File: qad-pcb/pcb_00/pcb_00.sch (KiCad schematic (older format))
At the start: 19 parts

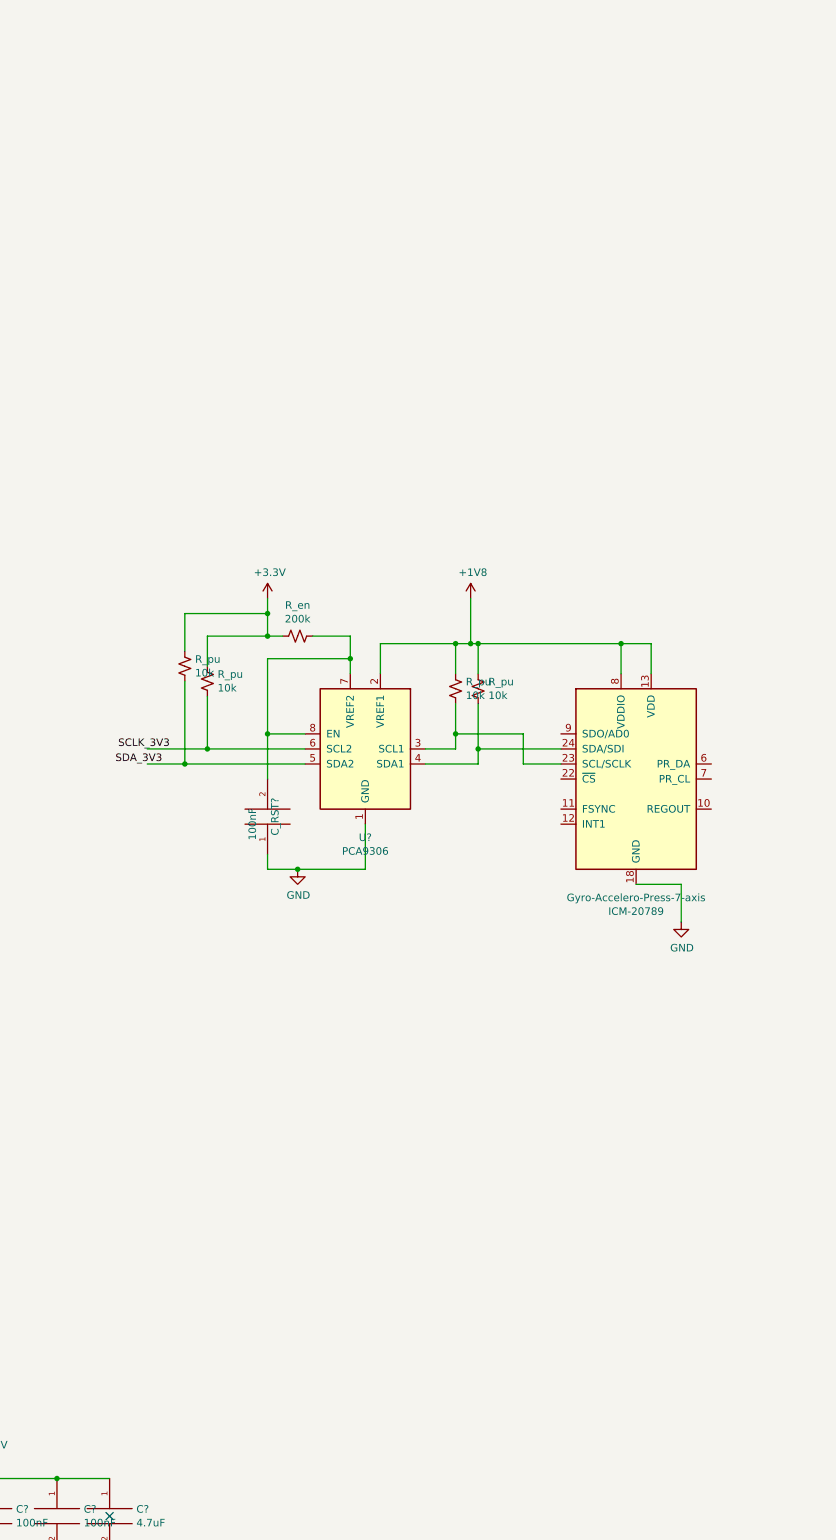
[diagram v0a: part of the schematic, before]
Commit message: Changed IMU :ICM-20789 -> BNO055
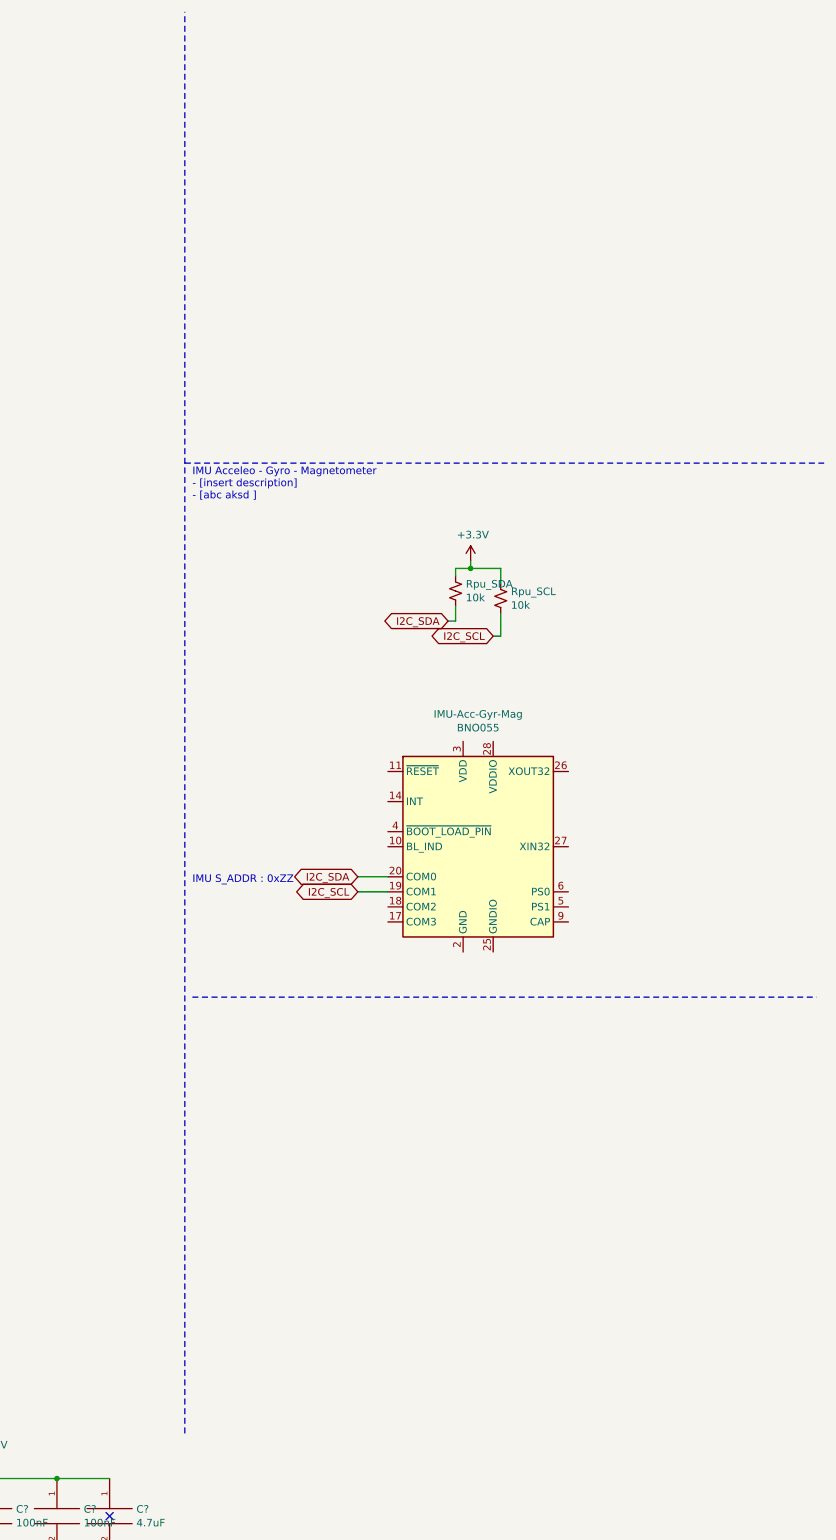
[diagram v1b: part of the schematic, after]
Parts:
- removed C_RST?: 100nF, symbol pspice:CAP
- removed Gyro-Accelero-Press-7-axis: ICM-20789, symbol my-qad-lib:ICM-20789
- removed R_en: 200k, symbol Device:R_Small_US
- removed R_pu (x4): 10k, symbol Device:R_Small_US
- removed U?: PCA9306, symbol Interface:PCA9306
- added IMU-Acc-Gyr-Mag: BNO055, Package_LGA:LGA-28_5.2x3.8mm_P0.5mm, symbol Sensor_Motion:BNO055
- added Rpu_SCL, Rpu_SDA: 10k, symbol Device:R_Small_US
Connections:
- net labels added: I2C_SCL, I2C_SDA
- net labels removed: +1V8, SCLK_3V3, SDA_3V3
- wire segments 82 -> 46
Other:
- note added: "IMU Acceleo - Gyro - Magnetometer\n- [insert description]\n- [abc aksd ]"
- note added: "IMU S_ADDR : 0xZZ"

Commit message: sch updated
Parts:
- gave numbers to parts that had none: 7
- renumbered C_RST to C_RST1, IMU-Acc-Gyr-Mag to IMU-Acc-Gyr-Mag1, R_RST to R_RST2, Rpu_SCL to Rpu_SCL1, Rpu_SDA to Rpu_SDA1, SW_RST to SW_RST1
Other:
- moved on the sheet: C1, C2, C3, C4, C5, C_RST1, IMU-Acc-Gyr-Mag1, R_RST1, R_RST2, Rpu_SCL1, Rpu_SDA1, SW_BOOT0A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
